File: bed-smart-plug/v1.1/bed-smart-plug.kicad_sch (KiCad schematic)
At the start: 36 parts, among them J1 3.5mm headphone jack, J2 Main + Sorties, Q1 BT136-600E, Q2 BT136-600E, Q3 BT136-600E, Q4 BT136-600E, U1 ESP32-POE, U2 QAM-RX10-433, U3 MOC3021M, U4 MOC3021M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

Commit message: update footprint
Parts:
- U2: footprint mylife-footprints:AMRX12A433P -> mylife-footprints:QAM-RX10-433
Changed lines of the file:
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@@
       (effects (font (size 1.27 1.27)))
     )
-    (property "Footprint" "mylife-footprints:AMRX12A433P" (at 83.82 138.43 0)
+    (property "Footprint" "mylife-footprints:QAM-RX10-433" (at 83.82 138.43 0)
       (effects (font (size 1.27 1.27)) hide)
     )

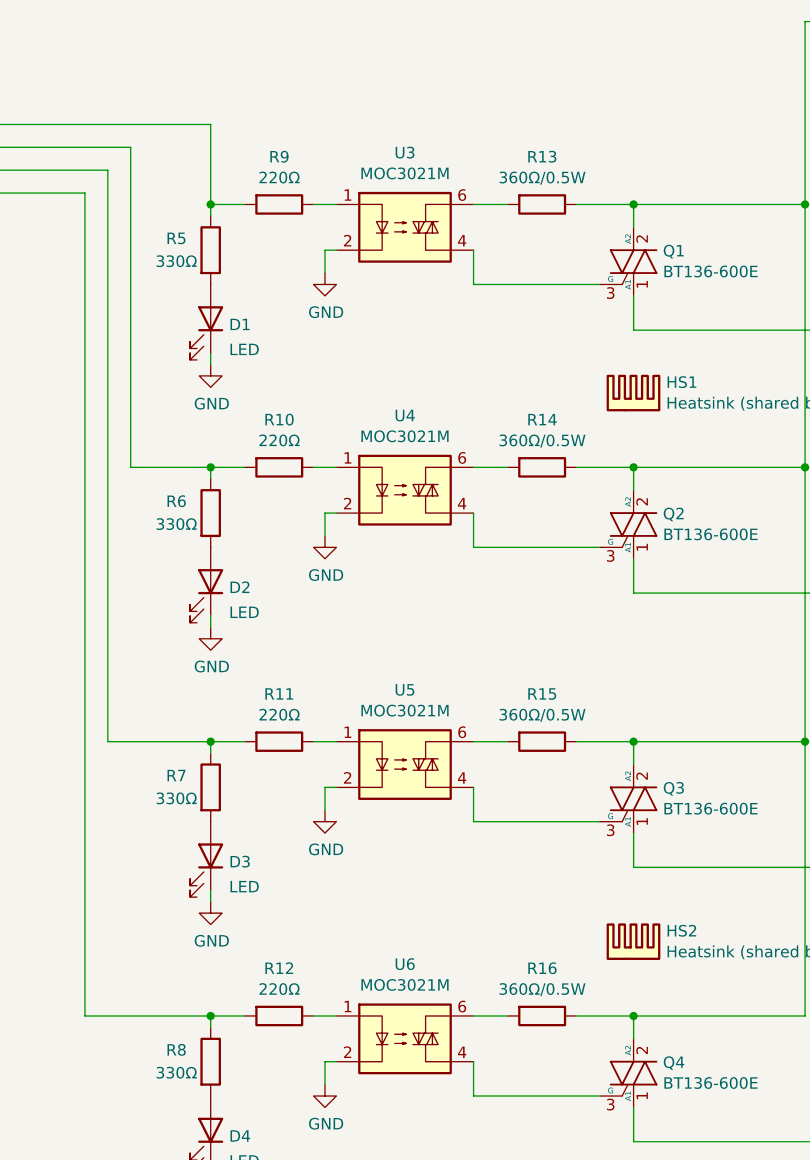
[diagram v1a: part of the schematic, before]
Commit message: update moc3021 to available part
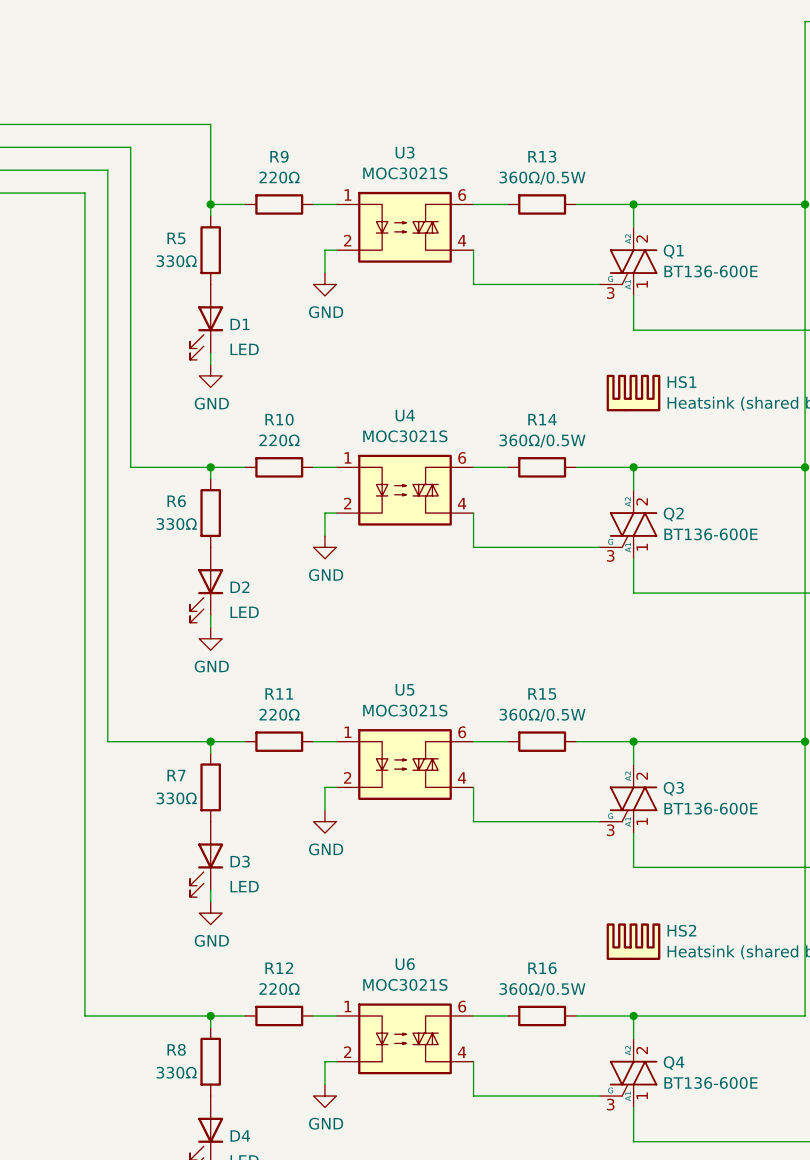
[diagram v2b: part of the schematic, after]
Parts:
- U3, U4, U5, U6: value MOC3021M -> MOC3021S; LCSC C108500 -> C427436
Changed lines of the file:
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@@
       (effects (font (size 1.27 1.27)))
     )
-    (property "Value" "MOC3021M" (at 166.37 37.2364 0)
+    (property "Value" "MOC3021S" (at 166.37 37.2364 0)
       (effects (font (size 1.27 1.27)))
     )
@@
       (effects (font (size 1.27 1.27) italic) (justify left) hide)
     )
-    (property "Datasheet" "https://jlcpcb.com/partdetail/Onsemi-MOC3021SM/C108500" (at 165.735 43.18 0)
+    (property "Datasheet" "https://jlcpcb.com/partdetail/liteon-MOC3021S/C427436" (at 165.735 43.18 0)
       (effects (font (size 1.27 1.27)) (justify left) hide)
     )
-    (property "LCSC" "C108500" (at 166.37 43.18 0)
+    (property "LCSC" "C427436" (at 166.37 43.18 0)
       (effects (font (size 1.27 1.27)) hide)
     )
@@
       (effects (font (size 1.27 1.27)))
     )
-    (property "Value" "MOC3021M" (at 166.37 127.4064 0)
+    (property "Value" "MOC3021S" (at 166.37 127.4064 0)
       (effects (font (size 1.27 1.27)))
     )
@@
       (effects (font (size 1.27 1.27) italic) (justify left) hide)
     )
-    (property "Datasheet" "https://jlcpcb.com/partdetail/Onsemi-MOC3021SM/C108500" (at 165.735 133.35 0)
+    (property "Datasheet" "https://jlcpcb.com/partdetail/liteon-MOC3021S/C427436" (at 165.735 133.35 0)
       (effects (font (size 1.27 1.27)) (justify left) hide)
     )
-    (property "LCSC" "C108500" (at 166.37 133.35 0)
+    (property "LCSC" "C427436" (at 166.37 133.35 0)
       (effects (font (size 1.27 1.27)) hide)
     )
@@
       (effects (font (size 1.27 1.27)))
     )
-    (property "Value" "MOC3021M" (at 166.37 96.9264 0)
+    (property "Value" "MOC3021S" (at 166.37 96.9264 0)
       (effects (font (size 1.27 1.27)))
     )
@@
       (effects (font (size 1.27 1.27) italic) (justify left) hide)
     )
-    (property "Datasheet" "https://jlcpcb.com/partdetail/Onsemi-MOC3021SM/C108500" (at 165.735 102.87 0)
+    (property "Datasheet" "https://jlcpcb.com/partdetail/liteon-MOC3021S/C427436" (at 165.735 102.87 0)
       (effects (font (size 1.27 1.27)) (justify left) hide)
     )
-    (property "LCSC" "C108500" (at 166.37 102.87 0)
+    (property "LCSC" "C427436" (at 166.37 102.87 0)
       (effects (font (size 1.27 1.27)) hide)
     )
@@
       (effects (font (size 1.27 1.27)))
     )
-    (property "Value" "MOC3021M" (at 166.37 66.4464 0)
+    (property "Value" "MOC3021S" (at 166.37 66.4464 0)
       (effects (font (size 1.27 1.27)))
     )
@@
       (effects (font (size 1.27 1.27) italic) (justify left) hide)
     )
-    (property "Datasheet" "https://jlcpcb.com/partdetail/Onsemi-MOC3021SM/C108500" (at 165.735 72.39 0)
+    (property "Datasheet" "https://jlcpcb.com/partdetail/liteon-MOC3021S/C427436" (at 165.735 72.39 0)
       (effects (font (size 1.27 1.27)) (justify left) hide)
     )
-    (property "LCSC" "C108500" (at 166.37 72.39 0)
-      (effects (font (size 1.27 1.27)) hide)
-    )
+    (property "LCSC" "C427436" (at 166.37 72.39 0)
+      (effects (font (size 1.27 1.27)) hide)
+    )
